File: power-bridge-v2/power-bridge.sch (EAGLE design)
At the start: 3 parts, among them X2 CON-MA03-2PCB_EDGE

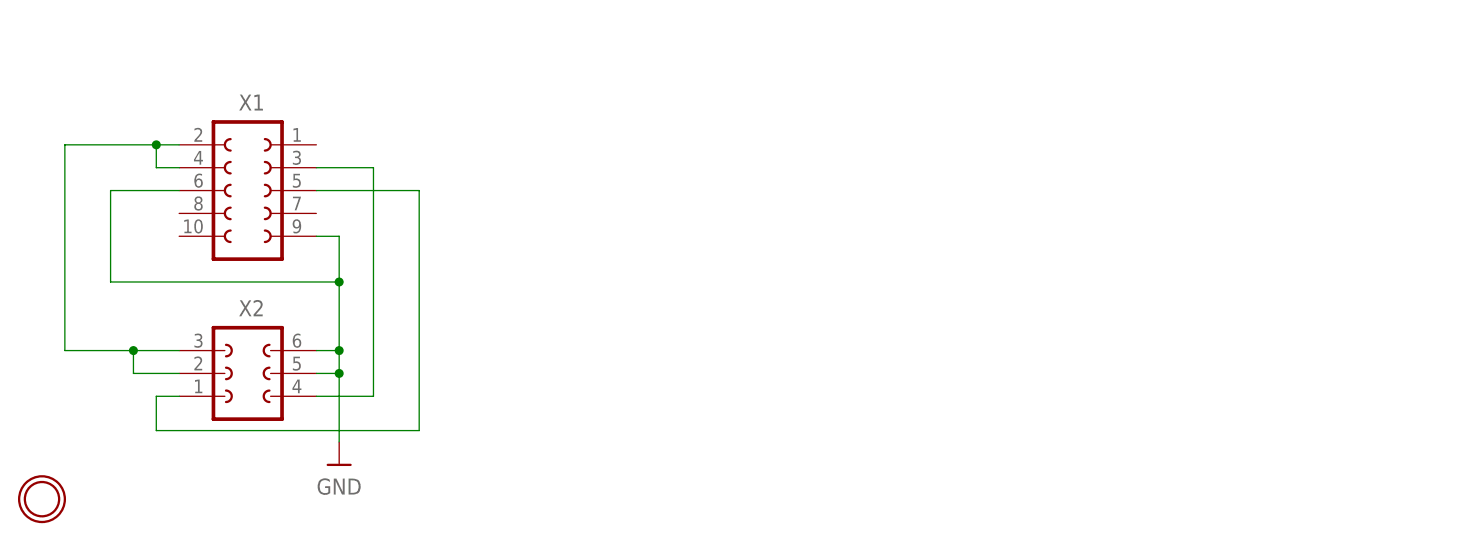
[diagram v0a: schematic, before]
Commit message: Add power bridge v3
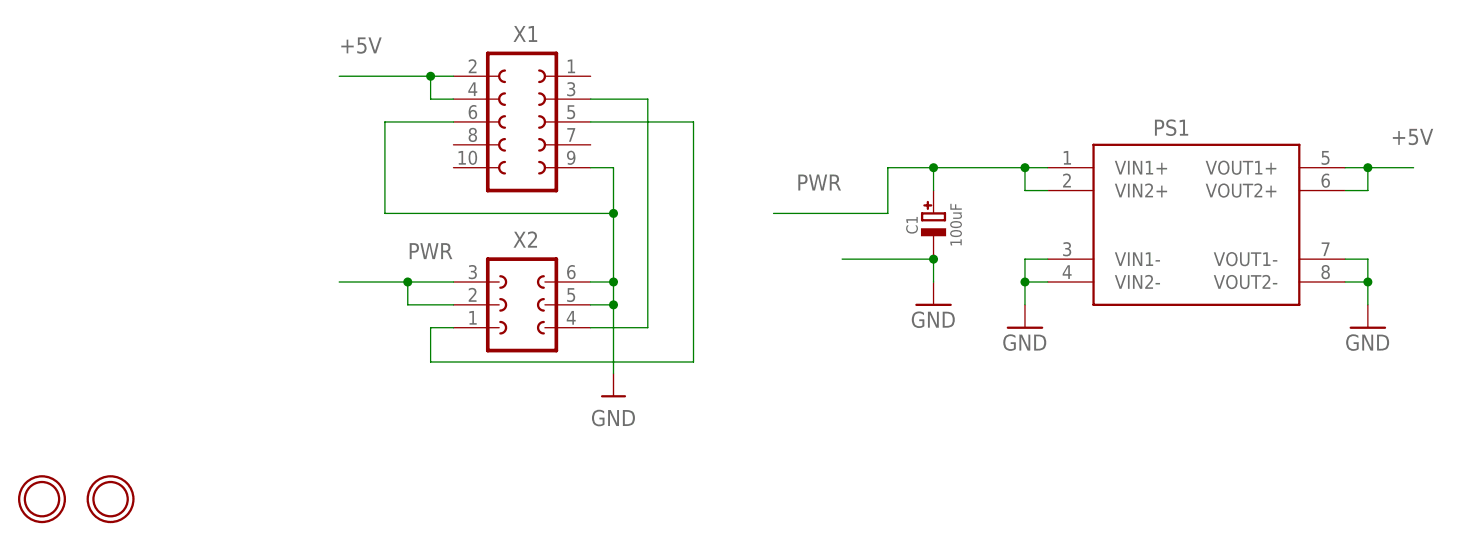
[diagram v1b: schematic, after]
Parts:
- added C1: 100uF, sanisimov:CAP_ELECTROLYTICPTH_3.5MMGRID_8MMDIA
- added PS1: (no value), sanisimov:K8801MODULE
- added U$3: MOUNTINGHOLE2.7_THICK, sanisimov:MOUNTINGHOLE2.7_THICK
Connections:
- new net +5V: PS1.VOUT1+, PS1.VOUT2+, X1.2, X1.4
- net GND: now also C1.-, PS1.VIN1-, PS1.VIN2-, PS1.VOUT1-, PS1.VOUT2-
- net PWR: now also C1.+, PS1.VIN1+, PS1.VIN2+; no longer X1.2, X1.4
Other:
- moved on the sheet: X1, X2
